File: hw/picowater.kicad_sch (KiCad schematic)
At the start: 20 parts, among them J1 GPIO Pins, J2 Power In, J3 +5V Pins, J4 UART, J5 Power Out, J6 RTC, U1 Pico

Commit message: update pcb
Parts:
- added J7: GPIO2, Connector_PinHeader_2.54mm:PinHeader_1x06_P2.54mm_Vertical, symbol Connector:Conn_01x06_Pin
- added JP1: VCC solder jump, Jumper:SolderJumper-2_P1.3mm_Open_Pad1.0x1.5mm, symbol Jumper:SolderJumper_2_Open
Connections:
- net GND: now also J7.1 (Pin_1)
- net SQW: now also U1.19 (GPIO14); no longer U1.15 (GPIO11)
- net at J6.2 (Pin_2): now also JP1.1 (A); no longer U1.14 (GPIO10)
- net at U1.24 (GPIO18): now also J7.2 (Pin_2)
- net at U1.25 (GPIO19): now also J7.3 (Pin_3)
- net at U1.26 (GPIO20): now also J7.4 (Pin_4)
- net at U1.27 (GPIO21): now also J7.5 (Pin_5)
- net at U1.29 (GPIO22): now also J7.6 (Pin_6)
- new net VCC: JP1.2 (B), U1.14 (GPIO10)
- no-connect marks 16 -> 11
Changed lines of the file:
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@@
   (no_connect (at 170.18 77.47))
   (no_connect (at 170.18 69.85))
-  (no_connect (at 170.18 90.17))
   (no_connect (at 170.18 82.55))
   (no_connect (at 134.62 105.41))
-  (no_connect (at 170.18 97.79))
-  (no_connect (at 170.18 85.09))
-  (no_connect (at 170.18 92.71))
   (no_connect (at 170.18 64.77))
-  (no_connect (at 170.18 95.25))
+  (no_connect (at 134.62 92.71))
   (no_connect (at 134.62 85.09))
   (no_connect (at 149.86 110.49))
-  (no_connect (at 134.62 102.87))
   (no_connect (at 170.18 72.39))
   (no_connect (at 170.18 57.15))
@@
     (stroke (width 0) (type default))
   )
+  (wire (pts (xy 170.18 97.79) (xy 186.69 97.79))
+    (stroke (width 0) (type default))
+  )
   (wire (pts (xy 173.99 59.69) (xy 179.07 59.69))
     (stroke (width 0) (type default))
@@
     (stroke (width 0) (type default))
   )
+  (wire (pts (xy 170.18 92.71) (xy 181.61 92.71))
+    (stroke (width 0) (type default))
+  )
   (wire (pts (xy 160.02 36.83) (xy 162.56 36.83))
     (stroke (width 0) (type default))
@@
     (stroke (width 0) (type default))
   )
+  (wire (pts (xy 184.15 92.71) (xy 193.04 92.71))
+    (stroke (width 0) (type default))
+  )
   (wire (pts (xy 22.86 76.2) (xy 31.75 76.2))
     (stroke (width 0) (type default))
@@
     (stroke (width 0) (type default))
   )
+  (wire (pts (xy 193.04 97.79) (xy 191.77 97.79))
+    (stroke (width 0) (type default))
+  )
   (wire (pts (xy 170.18 59.69) (xy 173.99 59.69))
     (stroke (width 0) (type default))
@@
     (stroke (width 0) (type default))
   )
+  (wire (pts (xy 111.76 90.17) (xy 134.62 90.17))
+    (stroke (width 0) (type default))
+  )
   (wire (pts (xy 170.18 102.87) (xy 180.34 102.87))
     (stroke (width 0) (type default))
@@
     (stroke (width 0) (type default))
   )
+  (wire (pts (xy 186.69 95.25) (xy 193.04 95.25))
+    (stroke (width 0) (type default))
+  )
   (wire (pts (xy 173.99 53.34) (xy 173.99 59.69))
     (stroke (width 0) (type default))
@@
     (stroke (width 0) (type default))
   )
+  (wire (pts (xy 170.18 95.25) (xy 184.15 95.25))
+    (stroke (width 0) (type default))
+  )
   (wire (pts (xy 82.55 76.2) (xy 82.55 68.58))
     (stroke (width 0) (type default))
@@
     (stroke (width 0) (type default))
   )
+  (wire (pts (xy 186.69 97.79) (xy 186.69 95.25))
+    (stroke (width 0) (type default))
+  )
+  (wire (pts (xy 181.61 92.71) (xy 181.61 90.17))
+    (stroke (width 0) (type default))
+  )
   (wire (pts (xy 36.83 40.64) (xy 76.2 40.64))
     (stroke (width 0) (type default))
   )
-  (wire (pts (xy 125.73 86.36) (xy 125.73 92.71))
-    (stroke (width 0) (type default))
-  )
   (wire (pts (xy 107.95 87.63) (xy 123.19 87.63))
     (stroke (width 0) (type default))
@@
     (stroke (width 0) (type default))
   )
+  (wire (pts (xy 125.73 102.87) (xy 134.62 102.87))
+    (stroke (width 0) (type default))
+  )
+  (wire (pts (xy 181.61 90.17) (xy 193.04 90.17))
+    (stroke (width 0) (type default))
+  )
+  (wire (pts (xy 179.07 87.63) (xy 193.04 87.63))
+    (stroke (width 0) (type default))
+  )
   (wire (pts (xy 127 57.15) (xy 134.62 57.15))
     (stroke (width 0) (type default))
   )
+  (wire (pts (xy 125.73 86.36) (xy 125.73 102.87))
+    (stroke (width 0) (type default))
+  )
   (wire (pts (xy 54.61 66.04) (xy 60.96 66.04))
     (stroke (width 0) (type default))
@@
     (stroke (width 0) (type default))
   )
+  (wire (pts (xy 170.18 90.17) (xy 179.07 90.17))
+    (stroke (width 0) (type default))
+  )
   (wire (pts (xy 22.86 66.04) (xy 22.86 76.2))
     (stroke (width 0) (type default))
   )
-  (wire (pts (xy 125.73 92.71) (xy 134.62 92.71))
-    (stroke (width 0) (type default))
-  )
-  (wire (pts (xy 102.87 90.17) (xy 134.62 90.17))
+  (wire (pts (xy 102.87 90.17) (xy 104.14 90.17))
     (stroke (width 0) (type default))
   )
@@
     (stroke (width 0) (type default))
   )
+  (wire (pts (xy 179.07 90.17) (xy 179.07 87.63))
+    (stroke (width 0) (type default))
+  )
   (wire (pts (xy 41.91 76.2) (xy 54.61 76.2))
     (stroke (width 0) (type default))
   )
+  (wire (pts (xy 184.15 95.25) (xy 184.15 92.71))
+    (stroke (width 0) (type default))
+  )
   (wire (pts (xy 160.02 40.64) (xy 160.02 36.83))
     (stroke (width 0) (type default))
@@
   )
   (wire (pts (xy 120.65 95.25) (xy 134.62 95.25))
+    (stroke (width 0) (type default))
+  )
+  (wire (pts (xy 170.18 85.09) (xy 193.04 85.09))
     (stroke (width 0) (type default))
   )
@@
     (effects (font (size 1.27 1.27)) (justify left bottom))
   )
-  (label "SQW" (at 127 92.71 0) (fields_autoplaced)
+  (label "VCC" (at 127 90.17 0) (fields_autoplaced)
+    (effects (font (size 1.27 1.27)) (justify left bottom))
+  )
+  (label "SQW" (at 127 102.87 0) (fields_autoplaced)
     (effects (font (size 1.27 1.27)) (justify left bottom))
   )
@@
     )
   )
+  (symbol (lib_id "Connector:Conn_01x06_Pin") (at 198.12 92.71 180) (unit 1)
+    (in_bom yes) (on_board yes) (dnp no)
+    (property "Reference" "J7" (at 196.85 92.71 0)
+      (effects (font (size 1.27 1.27)) (justify left))
+    )
+    (property "Value" "GPIO2" (at 198.12 82.55 0)
+      (effects (font (size 1.27 1.27)) (justify left))
+    )
+    (property "Footprint" "Connector_PinHeader_2.54mm:PinHeader_1x06_P2.54mm_Vertical" (at 198.12 92.71 0)
+      (effects (font (size 1.27 1.27)) hide)
+    )
+    (property "Datasheet" "~" (at 198.12 92.71 0)
+      (effects (font (size 1.27 1.27)) hide)
+    )
+    (pin "1")
+    (pin "2")
+    (pin "3")
+    (pin "4")
+    (pin "5")
+    (pin "6")
+    (instances
+      (project "picowater"
+        (path "/6f0795e9-9bd6-4197-b73a-51dca38e6e36"
+          (reference "J7") (unit 1)
+        )
+      )
+    )
+  )
   (symbol (lib_id "Connector_Generic_MountingPin:Conn_01x02_MountingPin") (at 17.78 63.5 0) (mirror y) (unit 1)
     (in_bom yes) (on_board yes) (dnp no)
@@
     )
   )
+  (symbol (lib_id "power:GND") (at 191.77 97.79 270) (unit 1)
+    (in_bom yes) (on_board yes) (dnp no)
+    (property "Reference" "#PWR023" (at 185.42 97.79 0)
+      (effects (font (size 1.27 1.27)) hide)
+    )
+    (property "Value" "GND" (at 187.96 95.25 0)
+      (effects (font (size 1.27 1.27)) (justify left))
+    )
+    (property "Footprint" "" (at 191.77 97.79 0)
+      (effects (font (size 1.27 1.27)) hide)
+    )
+    (property "Datasheet" "" (at 191.77 97.79 0)
+      (effects (font (size 1.27 1.27)) hide)
+    )
+    (pin "1")
+    (instances
+      (project "picowater"
+        (path "/6f0795e9-9bd6-4197-b73a-51dca38e6e36"
+          (reference "#PWR023") (unit 1)
+        )
+      )
+      (project "ISA rev7"
+        (path "/d1f04949-fb9b-4268-b5f3-6258a63d79ac"
+          (reference "#PWR021") (unit 1)
+        )
+      )
+    )
+  )
   (symbol (lib_id "power:GND") (at 121.92 40.64 0) (unit 1)
     (in_bom yes) (on_board yes) (dnp no) (fields_autoplaced)
@@
         )
       )
+    )
+  )
+  (symbol (lib_id "Jumper:SolderJumper_2_Open") (at 107.95 90.17 0) (unit 1)
+    (in_bom yes) (on_board yes) (dnp no)
+    (property "Reference" "JP1" (at 107.95 92.71 0)
+      (effects (font (size 1.27 1.27)))
+    )
+    (property "Value" "VCC solder jump" (at 107.95 95.25 0)
+      (effects (font (size 1.27 1.27)))
+    )
+    (property "Footprint" "Jumper:SolderJumper-2_P1.3mm_Open_Pad1.0x1.5mm" (at 107.95 90.17 0)
+      (effects (font (size 1.27 1.27)) hide)
+    )
+    (property "Datasheet" "~" (at 107.95 90.17 0)
+      (effects (font (size 1.27 1.27)) hide)
+    )
+    (pin "1")
+    (pin "2")
+    (instances
+      (project "picowater"
+        (path "/6f0795e9-9bd6-4197-b73a-51dca38e6e36"
+          (reference "JP1") (unit 1)
+        )
+      )

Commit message: [hw] update pcb
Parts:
- added J8: +3.3V Pins, Connector_PinHeader_2.54mm:PinHeader_1x03_P2.54mm_Vertical, symbol Connector:Conn_01x03_Pin
- R1, R2: footprint Resistor_THT:R_Axial_DIN0204_L3.6mm_D1.6mm_P5.08mm_Horizontal -> Resistor_THT:R_Axial_DIN0204_L3.6mm_D1.6mm_P7.62mm_Horizontal
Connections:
- net +3.3V: now also J8.2 (Pin_2), J8.3 (Pin_3)
- net +5V: now also J7.6 (Pin_6)
- net GND: now also J8.1 (Pin_1)
- net at U1.29 (GPIO22): no longer J7.6 (Pin_6)
- net ADC1: now reaches U1.32 (GPIO27_ADC1)
- net ADC1: now also J1.9 (Pin_9)
- net ADC2: now reaches U1.34 (GPIO28_ADC2)
- net ADC2: now also J1.8 (Pin_8)
- net GPIO7: no longer names the net of U1.10 (GPIO7)
- net GPIO7: no longer J1.8 (Pin_8)
- net GPIO8: no longer names the net of U1.11 (GPIO8)
- net GPIO8: no longer J1.9 (Pin_9)
- no-connect marks 11 -> 12
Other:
- moved on the sheet: J7

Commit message: [hw] v0.3 release
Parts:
- removed J8: +3.3V Pins, Connector_PinHeader_2.54mm:PinHeader_1x03_P2.54mm_Vertical, symbol Connector:Conn_01x03_Pin
- J1: footprint Connector_PinHeader_2.54mm:PinHeader_1x09_P2.54mm_Vertical -> Connector_PinHeader_2.54mm:PinHeader_2x09_P2.54mm_Vertical; symbol Connector:Conn_01x09_Pin -> Connector_Generic:Conn_02x09_Top_Bottom
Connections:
- net +3.3V: now also J1.1 (Pin_1)
- net ADC1: now also J1.17 (Pin_17); no longer J1.9 (Pin_9)
- net ADC2: now also J1.15 (Pin_15); no longer J1.8 (Pin_8)
- net GND: now also J1.10 (Pin_10), J1.12 (Pin_12), J1.14 (Pin_14), J1.16 (Pin_16), J1.18 (Pin_18), J1.2 (Pin_2), J1.4 (Pin_4), J1.6 (Pin_6), J1.8 (Pin_8); no longer J1.1 (Pin_1)
- net GPIO1: now also J1.3 (Pin_3); no longer J1.2 (Pin_2)
- net GPIO2: now also J1.5 (Pin_5); no longer J1.3 (Pin_3)
- net GPIO3: now also J1.7 (Pin_7); no longer J1.4 (Pin_4)
- net GPIO4: now also J1.9 (Pin_9); no longer J1.5 (Pin_5)
- net GPIO5: now also J1.11 (Pin_11); no longer J1.6 (Pin_6)
- net GPIO6: now also J1.13 (Pin_13); no longer J1.7 (Pin_7)

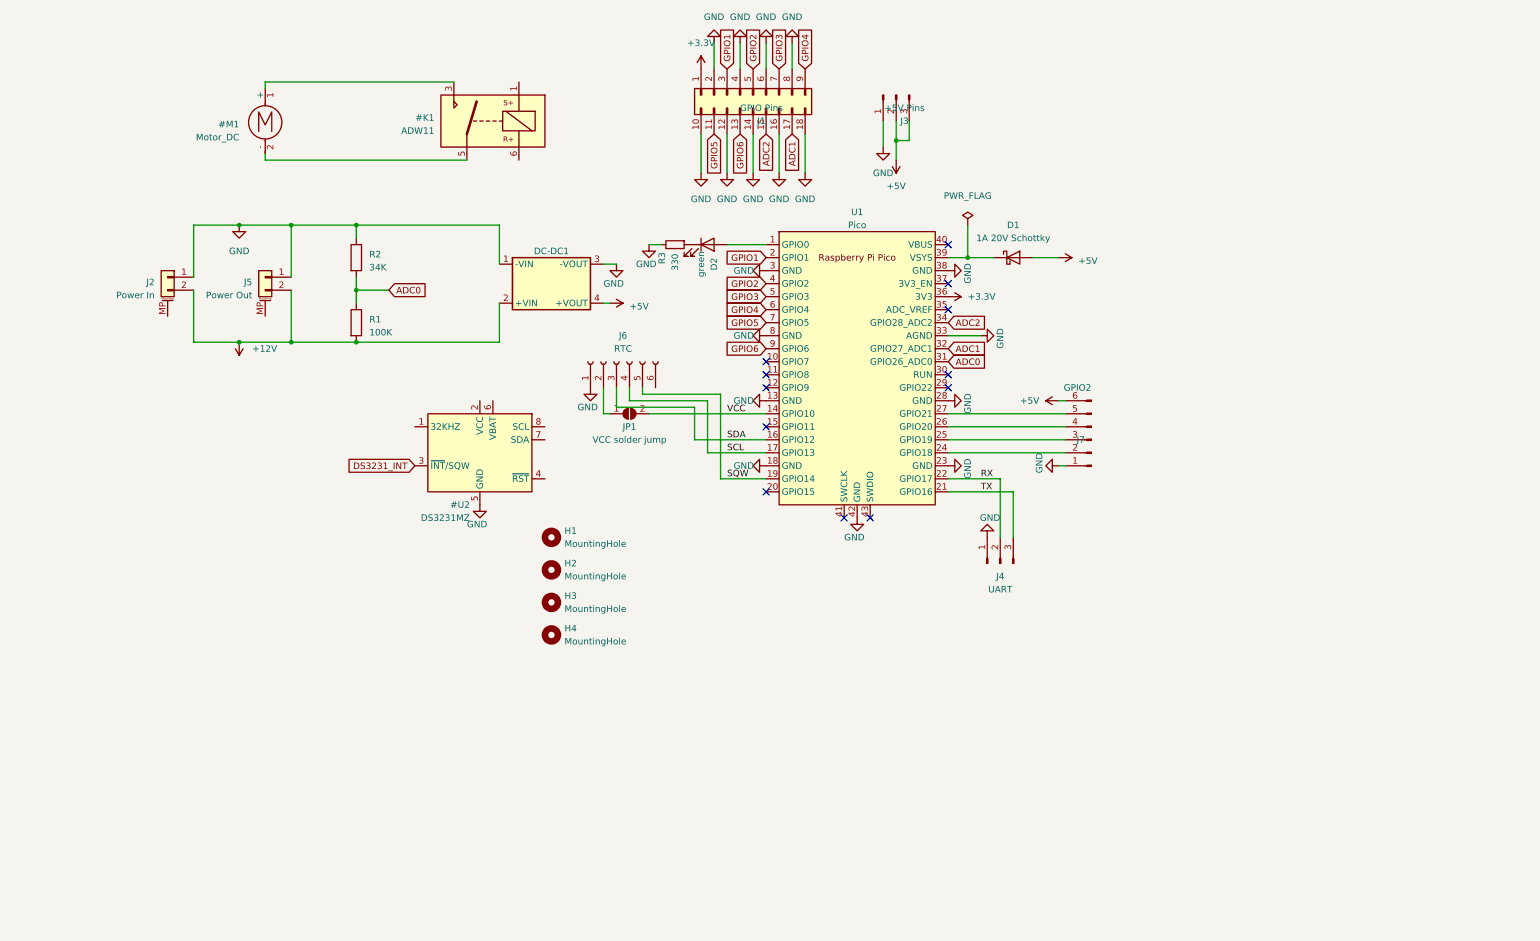
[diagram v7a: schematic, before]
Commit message: [pcb] new 0.9 release with many changes
- onboard DC-DC converter
- onboard RTC
- onboard Relay circuit
- new connectors
- others
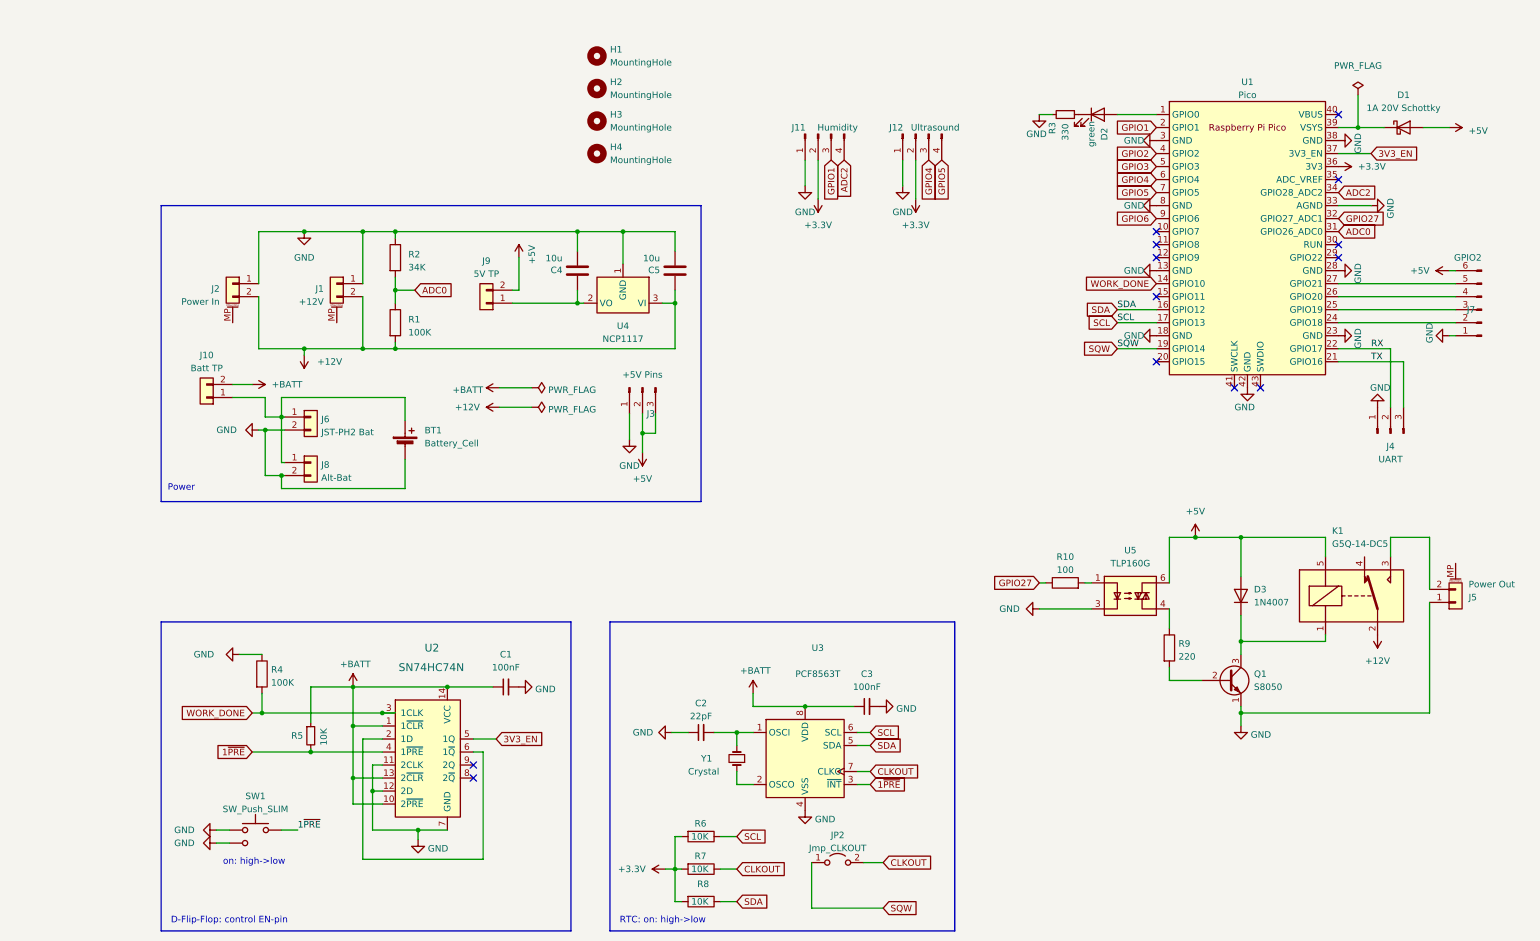
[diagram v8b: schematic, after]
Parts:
- removed #K1: ADW11, Relay_THT:Relay_1P1T_NO_10x24x18.8mm_Panasonic_ADW11xxxxW_THT, symbol Relay:ADW11
- removed #M1: Motor_DC, symbol Motor:Motor_DC
- removed #U2: DS3231MZ, Package_SO:SOIC-8_3.9x4.9mm_P1.27mm, symbol Timer_RTC:DS3231MZ
- removed DC-DC1: ~, Lunasys_Library:MP1584EN DC-DC 3A Step-Down, symbol Lunasys_Library:DC-DC_converter_MP1584EN_module
- removed J1: GPIO Pins, Connector_PinHeader_2.54mm:PinHeader_2x09_P2.54mm_Vertical, symbol Connector_Generic:Conn_02x09_Top_Bottom
- removed J6: RTC, Connector_PinSocket_2.54mm:PinSocket_1x06_P2.54mm_Horizontal, symbol Connector:Conn_01x06_Socket
- removed JP1: VCC solder jump, Jumper:SolderJumper-2_P1.3mm_Open_Pad1.0x1.5mm, symbol Jumper:SolderJumper_2_Open
- added BT1: Battery_Cell, Battery:Battery_Panasonic_CR2032-VS1N_Vertical_CircularHoles, symbol Device:Battery_Cell
- added C1, C3: 100nF, Capacitor_SMD:C_0402_1005Metric, symbol Device:C_Small
- added C2: 22pF, Capacitor_SMD:C_0402_1005Metric, symbol Device:C_Small
- added C4, C5: 10u, Capacitor_SMD:C_0805_2012Metric, symbol Device:C
- added D3: 1N4007, Diode_SMD:D_SOD-123, symbol Diode:1N4007
- added J1: +12V, Connector_PinSocket_2.54mm:PinSocket_1x02_P2.54mm_Vertical, symbol Connector_Generic_MountingPin:Conn_01x02_MountingPin
- added J10: Batt TP, Connector_PinHeader_2.54mm:PinHeader_1x02_P2.54mm_Vertical, symbol Connector_Generic:Conn_01x02
- added J11: Humidity, Connector_PinHeader_2.54mm:PinHeader_1x04_P2.54mm_Horizontal, symbol Connector:Conn_01x04_Pin
- added J12: Ultrasound, Connector_PinHeader_2.54mm:PinHeader_1x04_P2.54mm_Horizontal, symbol Connector:Conn_01x04_Pin
- added J6: JST-PH2 Bat, Connector_JST:JST_PH_S2B-PH-SM4-TB_1x02-1MP_P2.00mm_Horizontal, symbol Connector_Generic:Conn_01x02
- added J8: Alt-Bat, Connector_PinHeader_2.54mm:PinHeader_1x02_P2.54mm_Vertical, symbol Connector_Generic:Conn_01x02
- added J9: 5V TP, Connector_PinHeader_2.54mm:PinHeader_1x02_P2.54mm_Vertical, symbol Connector_Generic:Conn_01x02
- added JP2: Jmp_CLKOUT, Jumper:SolderJumper-2_P1.3mm_Open_Pad1.0x1.5mm, symbol Jumper:Jumper_2_Open
- added K1: G5Q-14-DC5, Relay_THT:Relay_SPDT_Omron-G5Q-1, symbol Relay:G5Q-1
- added Q1: S8050, Package_TO_SOT_SMD:TSOT-23, symbol Transistor_BJT:S8050
- added R10: 100, Resistor_SMD:R_0402_1005Metric, symbol Device:R
- added R4: 100K, Resistor_SMD:R_0402_1005Metric, symbol Device:R
- added R5: 10K, Resistor_SMD:R_0402_1005Metric, symbol Device:R_Small
- added R6, R7, R8: 10K, Resistor_SMD:R_0402_1005Metric, symbol Device:R
- added R9: 220, Resistor_SMD:R_0402_1005Metric, symbol Device:R
- added SW1: SW_Push_SLIM, Button_Switch_SMD:SW_Push_SPST_NO_Alps_SKRK, symbol user:SW_Push_SLIM
- added U2: SN74HC74N, Package_SO:SOIC-14_3.9x8.7mm_P1.27mm, symbol user:SN74HC74N
- added U3: PCF8563T, Package_SO:SOIC-8_3.9x4.9mm_P1.27mm, symbol Timer_RTC:PCF8563T
- added U4: NCP1117, Package_TO_SOT_SMD:SOT-223-3_TabPin2, symbol Regulator_Linear:NCP1117-5.0_SOT223
- added U5: TLP160G, Package_SO:MFSOP6-4_4.4x3.6mm_P1.27mm, symbol Relay_SolidState:TLP160G
- added Y1: Crystal, Crystal:Crystal_SMD_3215-2Pin_3.2x1.5mm, symbol Device:Crystal_Small
- D1: LCSC (none) -> C169527
- J2: footprint Connector_PinHeader_2.54mm:PinHeader_1x02_P2.54mm_Vertical -> Connector_BarrelJack:BarrelJack_CUI_PJ-102AH_Horizontal
- R1: footprint Resistor_THT:R_Axial_DIN0204_L3.6mm_D1.6mm_P7.62mm_Horizontal -> Resistor_SMD:R_0402_1005Metric; LCSC (none) -> C25741
- R2: footprint Resistor_THT:R_Axial_DIN0204_L3.6mm_D1.6mm_P7.62mm_Horizontal -> Resistor_SMD:R_0402_1005Metric; LCSC (none) -> C48939
- R3: LCSC (none) -> C3018003
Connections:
- net +12V: now also C5.1, J1.2 (Pin_2), K1.2, U4.3 (VI); no longer J5.2 (Pin_2)
- net +3.3V: now also J11.2 (Pin_2), J12.2 (Pin_2), R6.2, R7.2, R8.2
- net +5V: now also D3.2 (A), J9.2 (Pin_2), K1.5, U5.6
- net ADC2: now also J11.4 (Pin_4)
- net GND: now also BT1.2 (-), C1.2, C2.1, C3.2, C4.2, C5.2, J1.1 (Pin_1), J11.1 (Pin_1), J12.1 (Pin_1), J6.2 (Pin_2), J8.2 (Pin_2), Q1.1 (E), R4.1, SW1.1, SW1.3 (1), U2.11 (2CLK), U2.12 (2D), U2.7 (GND), U3.4 (VSS), U4.1 (GND), U5.3
- net GPIO1: now also J11.3 (Pin_3)
- net GPIO4: now also J12.3 (Pin_3)
- net GPIO5: now also J12.4 (Pin_4)
- net SCL: now also R6.1, U3.6 (SCL)
- net SDA: now also R8.1, U3.5 (SDA)
- net SQW: now also JP2.1 (A)
- net 3V3_EN: now reaches U1.37 (3V3_EN)
- net 3V3_EN: now also U2.5 (1Q)
- net ADC1 renamed GPIO27
- net GPIO27: now also R10.1
- net VCC renamed WORK_DONE
- net WORK_DONE: now also R4.2, U2.3 (1CLK)
- new net: U2.2 (1D), U2.6 (1~{Q})
- new net: BT1.1 (+), J10.1 (Pin_1), J6.1 (Pin_1), J8.1 (Pin_1)
- new net: D3.1 (K), K1.1, Q1.3 (C)
- new net: J5.2 (Pin_2), K1.3
- new net: U3.2 (OSCO), Y1.1
- new net: C2.2, U3.1 (OSCI), Y1.2
- new net: Q1.2 (B), R9.2
- new net: C4.1, J9.1 (Pin_1), U4.2 (VO)
- new net: R9.1, U5.4
- new net: R10.2, U5.1
- new net +BATT: C1.1, C3.1, J10.2 (Pin_2), R5.1, U2.1 (1~{CLR}), U2.10 (2~{PRE}), U2.13 (2~{CLR}), U2.14 (VCC), U3.8 (VDD)
- new net 1~{PRE}: R5.2, SW1.2, U2.4 (1~{PRE}), U3.3 (~{INT})
- new net CLKOUT: JP2.2 (B), R7.1, U3.7 (CLKO)
- no-connect marks 12 -> 13
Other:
- note added: "D-Flip-Flop: control EN-pin"
- note added: "Power"
- note added: "RTC: on: high->low"
- note added: "on: high->low"
- moved on the sheet: D1, D2, H1, H2, H3, H4, J2, J3, J4, J7, R1, R2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
